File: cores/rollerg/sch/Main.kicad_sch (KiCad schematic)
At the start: 1 part, among them U1 053248

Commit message: wip rollerg sch: objects page
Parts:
- added D19, D20: 74LS257, symbol 74xx:74LS257
- added F11, F12: PAL16L8, symbol Logic_Programmable:PAL16L8
- added F13: 74LS138, symbol 74xx:74LS138
- added G18: 74LS174, symbol 74xx:74LS174
- added I16: ~, symbol konami:053252
- added J14: 74LS245, symbol jt74:74LS245
- renumbered U1 to H11
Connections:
- net VSS: now reaches H11.1 (VSS)
- net VSS: now also H11.10 (VSS), H11.19 (VSS), H11.25 (VSS), H11.31 (R0), H11.32 (R1), H11.33 (R2), H11.34 (R3), H11.35 (R4), H11.36 (R5), H11.37 (R6), H11.42 (VSS), H11.47 (R7), H11.48 (TEST), H11.5 (R9), H11.52 (R8), H11.57 (VSS), I16.22 (SEL0), I16.23 (SEL1), I16.28 (VSS), I16.43 (SEL2), I16.6 (VSS)
- net MAIN_A3: now reaches H11.11 (A3)
- net MAIN_A2: now reaches H11.12 (A2)
- net MAIN_A1: now reaches H11.13 (A1)
- net MAIN_A0: now reaches H11.14 (A0)
- net R/~{W}: now reaches H11.15 (R/~{W})
- net ~{AS}: now reaches H11.16 (~{AS})
- net ~{DS}: now reaches H11.20 (~{DS})
- net MAIN_D0: now reaches H11.21 (D0)
- net MAIN_D1: now reaches H11.22 (D1)
- net MAIN_D2: now reaches H11.23 (D2)
- net MAIN_D3: now reaches H11.24 (D3)
- net MAIN_D4: now reaches H11.27 (D4)
- net MAIN_D5: now reaches H11.28 (D5)
- net MAIN_D6: now reaches H11.29 (D6)
- net MAIN_D7: now reaches H11.30 (D7)
- net MAIN_A16: now reaches H11.38 (A16)
- net MAIN_A17: now reaches H11.39 (A17)
- net MAIN_A18: now reaches H11.40 (A18)
- net MAIN_A19: now reaches H11.41 (A19)
- net MAIN_A20: now reaches H11.43 (A20)
- net MAIN_A21: now reaches H11.44 (A21)
- net MAIN_A22: now reaches H11.45 (A22)
- net MAIN_A23: now reaches H11.46 (A23)
- net MAIN_A15: now reaches H11.53 (A15)
- net MAIN_A14: now reaches H11.54 (A14)
- net MAIN_A13: now reaches H11.55 (A13)
- net MAIN_A12: now reaches H11.56 (A12)
- net MAIN_A11: now reaches H11.59 (A11)
- net MAIN_A7: now reaches H11.6 (A7)
- net MAIN_A10: now reaches H11.60 (A10)
- net MAIN_A9: now reaches H11.61 (A9)
- net MAIN_A8: now reaches H11.62 (A8)
- net MAIN_A6: now reaches H11.7 (A6)
- net MAIN_A5: now reaches H11.8 (A5)
- net MAIN_A4: now reaches H11.9 (A4)
- new net: D19.12 (Zc), G18.13 (D4), J14.6 (A4)
- new net: D19.4 (Za), J14.9 (A7)
- new net: D19.7 (Zb), J14.8 (A6)
- new net: D19.9 (Zd), G18.14 (D5), J14.7 (A5)
- new net: D20.12 (Zc), G18.3 (D0), J14.2 (A0)
- new net: D20.4 (Za), G18.11 (D3), J14.5 (A3)
- new net: D20.7 (Zb), G18.6 (D2), J14.4 (A2)
- new net: D20.9 (Zd), G18.4 (D1), J14.3 (A1)
- new net: F13.14 (O1), G18.9 (Cp)
- new net: F12.2 (I2), G18.7 (Q2)
- new net DB0: I16.13 (DB0)
- new net DB1: I16.14 (DB1)
- new net DB2: I16.15 (DB2)
- new net DB3: I16.16 (DB3)
- new net DB4: I16.18 (DB4)
- new net DB5: I16.19 (DB5)
- new net DB6: I16.20 (DB6)
- new net DB7: I16.21 (DB7)
- new net G18P15: G18.15 (Q5)
- new net VCC: D20.11 (I0d), D20.14 (I0c), D20.2 (I0a), D20.5 (I0b)
- new net ~{OBJ_CS}: F12.18 (IO2)

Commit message: wip rollerg sch: PSAC progress
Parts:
- added J16: 74LS04, symbol jt74:74LS04
- added J17: XTAL_OSC, symbol Device:Crystal_GND23_Small
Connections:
- net VCC: now also J17.3
- net VSS: now also J17.1, J17.2
- net CLK4: now reaches I16.11 (CLK4)
- net ~{VBK}: now reaches I16.27 (~{VBK})
- net ~{HBK}: now reaches I16.33 (~{HBK})
- net at I16.5 (CLK): now also J16.4
- net RES: now reaches I16.7 (RES)
- net CLK1: now reaches I16.8 (CLK1)
- net CLK2: now reaches I16.9 (CLK2)
- net PAL14: now reaches F12.14 (IO6)
- net OBJOE: now reaches F12.16 (IO4)
- net PAL17: now reaches F12.17 (I03)
- net OBJSE: now reaches F12.19 (IO1)
- new net 24CLK: J16.3, J17.4

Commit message: wip rollerg sch: PSAC
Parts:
- added C20, C21, C23: 74LS253, symbol 74xx:74LS253
- added D18, G16: 74LS32, symbol jt74:74LS32
- added DIPSW2: SW_DIP_x08, symbol Switch:SW_DIP_x08
- added F11: PAL16L8, symbol Logic_Programmable:PAL16L8
- added F14: 74LS04, symbol jt74:74LS04
- added F16: 74LS08, symbol 74xx:74LS08
- added RA4_7KX8: R_Network08_US, Resistor_THT:R_Array_SIP7, symbol Device:R_Network08_US
- added S1: 051550, symbol konami:051550
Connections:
- net MAIN_A0: now also D18.5, F14.3
- net MAIN_A10: now also F12.5 (I5)
- net MAIN_A11: now also F12.4 (I4)
- net MAIN_A12: now also F12.3 (I3)
- net MAIN_A4: now also F13.1 (A0)
- net MAIN_A5: now also F12.11 (I10), F13.2 (A1)
- net MAIN_A6: now also F12.9 (I9), F13.3 (A2)
- net MAIN_A7: now also F12.8 (I8)
- net MAIN_A8: now also F12.7 (I7)
- net MAIN_A9: now also F12.6 (I6)
- net OBJSE: now also D18.4
- net VCC: now also D19.11 (I0d), D19.14 (I0c), D19.5 (I0b), F13.6 (E3)
- net VSS: now also F13.5 (E2), C20.10 (I0b), C20.6 (I0a), C21.10 (I0b), C21.11 (I1b), C21.6 (I0a), C23.10 (I0b), C23.11 (I1b), C23.6 (I0a), S1.13 (VSS), S1.14 (VSS)
- net ~{DS}: now also D18.10
- net ~{OBJ_CS}: now also F16.10
- net at D19.1 (S): now also D20.1 (S), F14.4
- net at D19.10 (I1d): now also DIPSW2.11, RA4_7KX8.7 (R6)
- net MAIN_Z6: now reaches D19.12 (Zc), G18.13 (D4), J14.6 (A4)
- net at D19.13 (I1c): now also DIPSW2.12, RA4_7KX8.6 (R5)
- net ZOE: now reaches D19.15 (OE)
- net ZOE: now also F13.9 (O6)
- net CPU~{EN}: now reaches D19.2 (I0a)
- net CPU~{EN}: now also G16.2
- net at D19.3 (I1a): now also DIPSW2.9, RA4_7KX8.9 (R8)
- net MAIN_Z4: now reaches D19.4 (Za), J14.9 (A7)
- net at D19.6 (I1b): now also DIPSW2.10, RA4_7KX8.8 (R7)
- net MAIN_Z5: now reaches D19.7 (Zb), J14.8 (A6)
- net MAIN_Z7: now reaches D19.9 (Zd), G18.14 (D5), J14.7 (A5)
- net at D20.10 (I1d): now also DIPSW2.15, RA4_7KX8.3 (R2)
- net MAIN_Z2: now reaches D20.12 (Zc), G18.3 (D0), J14.2 (A0)
- net at D20.13 (I1c): now also DIPSW2.16, RA4_7KX8.2 (R1)
- net at D20.15 (OE): now also F11.9 (I9)
- net at D20.3 (I1a): now also DIPSW2.13, RA4_7KX8.5 (R4)
- net MAIN_Z0: now reaches D20.4 (Za), G18.11 (D3), J14.5 (A3)
- net at D20.6 (I1b): now also DIPSW2.14, RA4_7KX8.4 (R3)
- net MAIN_Z1: now reaches D20.7 (Zb), G18.6 (D2), J14.4 (A2)
- net MAIN_Z3: now reaches D20.9 (Zd), G18.4 (D1), J14.3 (A1)
- net CRES: now reaches I16.12 (CRES)
- net CRES: now also G18.1 (~{Mr})
- net DTAC: now reaches H11.49 (DTAC)
- net at F13.10 (O5): now also C20.1 (OEa), C20.15 (OEb), C21.1 (OEa), C21.15 (OEb), C23.1 (OEa), C23.15 (OEb)
- net PAL12: now reaches F13.4 (E1)
- net PAL12: now also F12.12 (IO8)
- net at J14.1 (A->B): now also G16.11
- net OBJRAMD7: now reaches J14.11 (B7)
- net OBJRAMD6: now reaches J14.12 (B6)
- net OBJRAMD5: now reaches J14.13 (B5)
- net OBJRAMD4: now reaches J14.14 (B4)
- net OBJRAMD3: now reaches J14.15 (B3)
- net OBJRAMD2: now reaches J14.16 (B2)
- net OBJRAMD1: now reaches J14.17 (B1)
- net OBJRAMD0: now reaches J14.18 (B0)
- net at J14.19 (~{CE}): now also G16.3
- net at F12.1 (I1): now also F11.12 (IO8)
- net PAL15: now reaches F12.15 (IO5)
- net PAL15: now also F14.5, F16.9
- net G18P7: now reaches F12.2 (I2), G18.7 (Q2)
- net at G18.2 (Q0): now also S1.15 (OUT1)
- net at G18.5 (Q1): now also S1.16 (OUT2)
- new net: F16.8, G16.1
- new net: F14.6, G16.12
- new net: D18.6, D18.9
- new net WR: D18.8
- new net ~{RD}: G16.13
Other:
- moved on the sheet: F11, F12

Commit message: wip rollerg sch: SOUND
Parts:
- removed C20, C21, C23: 74LS253, symbol 74xx:74LS253
- removed F11: PAL16L8, symbol Logic_Programmable:PAL16L8
- removed unit 3 of F14
- removed F16: 74LS08, symbol 74xx:74LS08
- removed G16: 74LS32, symbol jt74:74LS32
- removed J14: 74LS245, symbol jt74:74LS245
- added 7KX4: R_Network04_US, Resistor_THT:R_Array_SIP5, symbol Device:R_Network04_US
- added C18, D16: 74LS07, symbol 74xx:74LS07
- added F9: 74LS245, symbol jt74:74LS245
- added H14: 74LS367, symbol 74xx:74LS367
- added H16: 74LS04, symbol jt74:74LS04
- added JP2: Jumper_2_Open, symbol Jumper:Jumper_2_Open
- added R1: 222, symbol Device:R_US
- added R10, R17: 470, symbol Device:R_US
- added R11, R5: 100, symbol Device:R_US
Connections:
- net CRES: now also H14.4 (I2)
- net DB0: now also G18.3 (D0), F9.2 (A0)
- net DB1: now also G18.4 (D1), F9.3 (A1)
- net DB2: now also G18.6 (D2), F9.4 (A2)
- net DB3: now also G18.11 (D3), F9.5 (A3)
- net DB4: now also G18.13 (D4), F9.6 (A4)
- net DB5: now also G18.14 (D5), F9.7 (A5)
- net DB6: now also F9.8 (A6)
- net DB7: now also F9.9 (A7)
- net MAIN_A0: now also I16.42 (AB0)
- net MAIN_A1: now also I16.41 (AB1)
- net MAIN_A12: now also F11.5 (I5)
- net MAIN_A13: now also F11.4 (I4)
- net MAIN_A14: now also F11.3 (I3)
- net MAIN_A15: now also F11.2 (I2)
- net MAIN_A16: now also F11.9 (I9)
- net MAIN_A17: now also F11.8 (I8)
- net MAIN_A18: now also F11.7 (I7)
- net MAIN_A19: now also F11.6 (I6)
- net MAIN_A2: now also I16.40 (AB2)
- net MAIN_A3: now also I16.38 (AB3)
- net MAIN_D0: now also F9.18 (B0)
- net MAIN_D1: now also F9.17 (B1)
- net MAIN_D2: now also F9.16 (B2)
- net MAIN_D3: now also F9.15 (B3)
- net MAIN_D4: now also F9.14 (B4)
- net MAIN_D5: now also F9.13 (B5)
- net MAIN_D6: now also F9.12 (B6)
- net MAIN_D7: now also F9.11 (B7)
- net MAIN_Z0: no longer G18.11 (D3)
- net MAIN_Z1: no longer G18.6 (D2)
- net MAIN_Z2: no longer G18.3 (D0)
- net MAIN_Z3: no longer G18.4 (D1)
- net MAIN_Z6: no longer G18.13 (D4)
- net MAIN_Z7: no longer G18.14 (D5)
- net RES: now also S1.10 (~{RESET})
- net R/~{W}: now also F11.11 (I10), I16.37 (~{RW}), F9.1 (A->B)
- net VCC: now also D19.16 (VCC), D20.16 (VCC), F11.20 (VCC), F13.16 (VCC), H11.26 (VCC), H11.50 (EPA), H11.58 (VCC), I16.17 (VDD), I16.3 (~{HLDI}), I16.39 (VDD), I16.4 (~{VLDI}), 7KX4.1 (common), H14.16 (VCC), R10.2, R17.2
- net VSS: now also D19.8 (GND), D20.8 (GND), F11.10 (GND), F13.8 (GND), 7KX4.2 (R1), 7KX4.3 (R2), 7KX4.4 (R3), 7KX4.5 (R4), H14.1 (OEa), H14.8 (GND), R1.1
- net ZOE: now also D20.15 (OE)
- net ~{AS}: now also F11.1 (I1)
- net MOE: now reaches F13.10 (O5)
- net SMU: now reaches D19.1 (S), D20.1 (S), F14.4
- net ~{CS1}: now reaches F11.13 (IO7)
- net MAIN_AB0: now reaches F11.14 (IO6)
- net MAIN_AB1: now reaches F11.15 (IO5)
- net MAIN_AB2: now reaches F11.16 (IO4)
- net MAIN_AB3: now reaches F11.17 (I03)
- net at F11.18 (IO2): now also F9.19 (~{CE})
- net OOE: now reaches F11.19 (IO1)
- net PE: now reaches I16.1 (PE)
- net PE: now also H14.2 (I1)
- net PQ: now reaches I16.2 (PQ)
- net PQ: now also H16.5
- net at I16.25 (~{CSY}): now also D16.1
- net at I16.26 (~{VSY}): now also C18.5
- net ~{IRQ}: now reaches I16.34 (INT1)
- net ~{IRQ}: now also H11.4 (~{IRQ})
- net ~{CCO}: now reaches I16.36 (~{CC0})
- net ~{CCO}: now also F12.13 (IO7)
- net MPQ: now reaches H11.17 (PQ)
- net MPQ: now also H14.3 (O1a)
- net ~{CLK2}: now reaches H11.18 (CLK)
- net RESET: now reaches H11.2 (~{RESET})
- net RESET: now also H14.5 (O2a)
- net MPE: now reaches H11.51 (PE)
- net MPE: now also H14.7 (O3a)
- net RCLK: now reaches S1.1 (CLK)
- net RCLK: now also F13.13 (O2)
- net COIN_CNT_2: now reaches S1.20 (CNT2)
- net COIN_CNT_2: now also S1.21 (CNT2)
- net COIN_CNT_1: now reaches S1.22 (CNT1)
- net COIN_CNT_1: now also S1.23 (CNT1)
- net at S1.4 (VREF): now also JP2.2 (B)
- net at S1.5 (RES): now also JP2.1 (A)
- net at S1.7 (CT): now also R1.2
- net SND_INT: now reaches F13.11 (O4)
- net ~{MCS}: now reaches F13.12 (O3)
- new net: D16.2, R10.1, R5.1
- new net: H14.6 (I3), H16.6
- new net: C18.6, R11.1, R17.1
- new net SYNC: R5.2
- no-connect marks 0 -> 8
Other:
- note added: "PULL"
- moved on the sheet: D18B, D18C, D19, D20, DIPSW2, F11, F12, F13, F14B, G18, H11, I16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

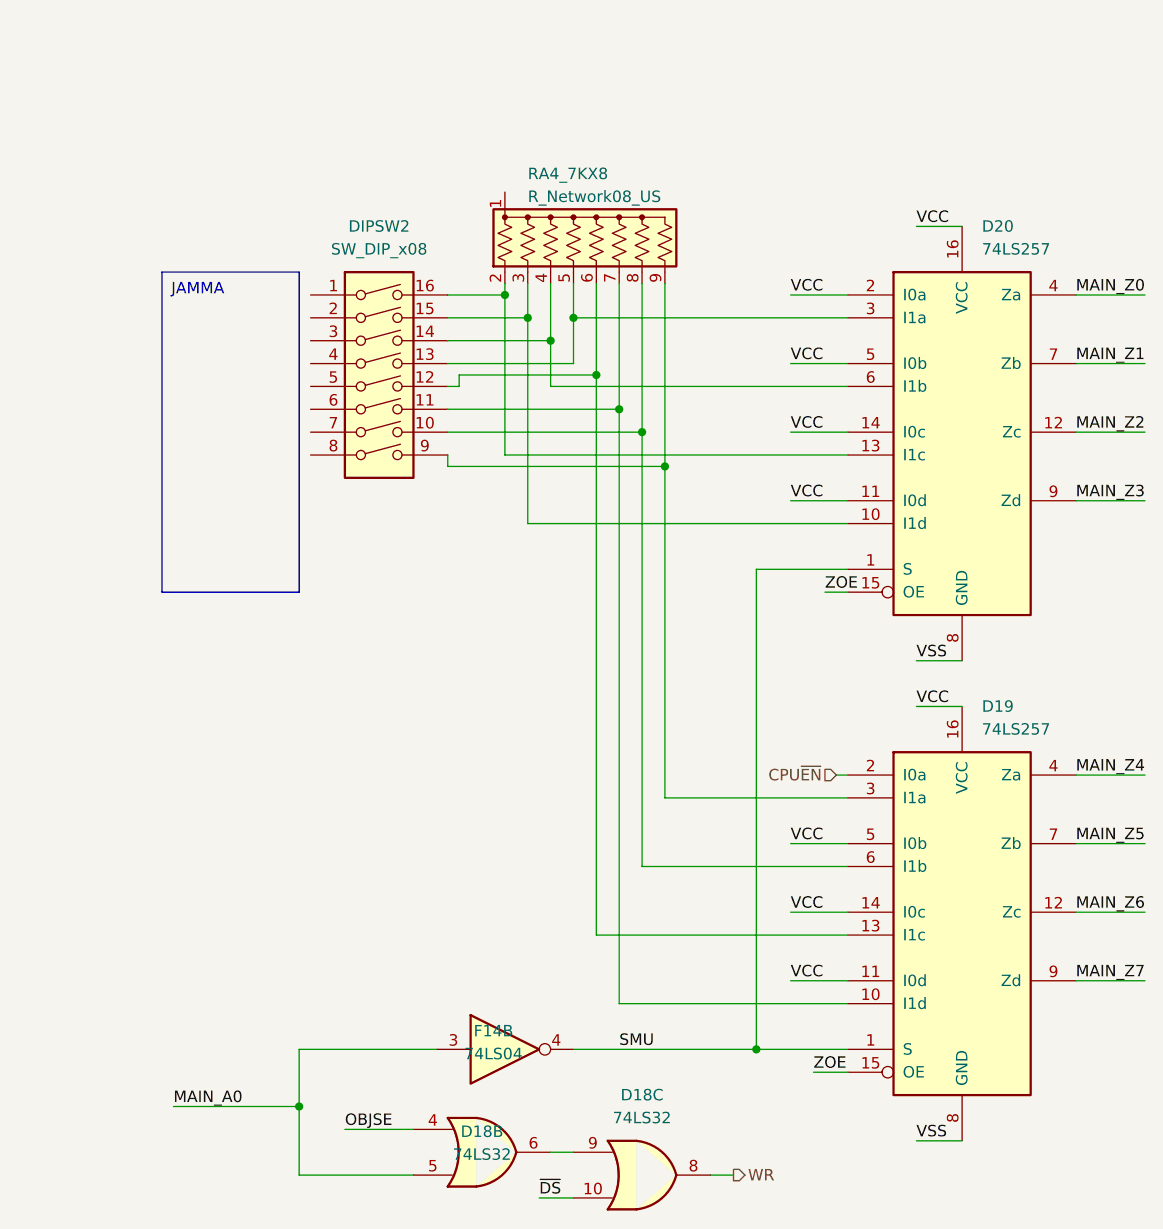
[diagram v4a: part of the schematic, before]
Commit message: wip rollerg sch: CABINET AND RGB
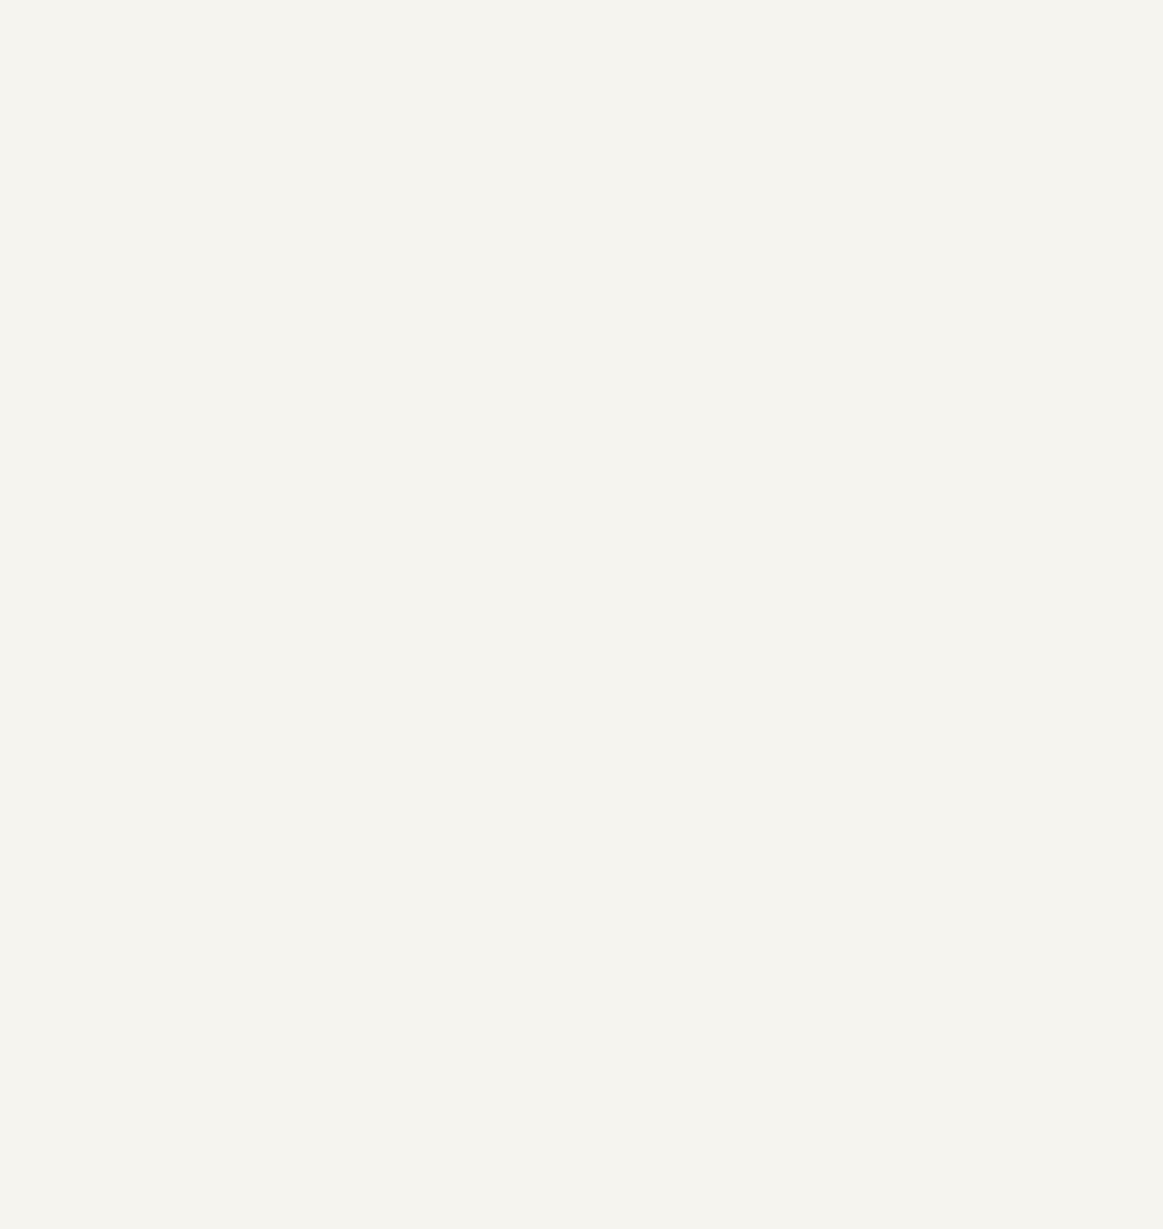
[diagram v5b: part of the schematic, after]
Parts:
- removed D18: 74LS32, symbol jt74:74LS32
- removed D19, D20: 74LS257, symbol 74xx:74LS257
- removed DIPSW2: SW_DIP_x08, symbol Switch:SW_DIP_x08
- removed F14: 74LS04, symbol jt74:74LS04
- removed RA4_7KX8: R_Network08_US, Resistor_THT:R_Array_SIP7, symbol Device:R_Network08_US

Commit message: almost complete rollerg sch
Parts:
- removed 7KX4: R_Network04_US, Resistor_THT:R_Array_SIP5, symbol Device:R_Network04_US
- removed R1: 222, symbol Device:R_US
- added C6: 100k, Capacitor_THT:C_Axial_L3.8mm_D2.6mm_P10.00mm_Horizontal, symbol Device:C
- added RN7: R_Network08_US, Resistor_THT:R_Array_SIP9, symbol Device:R_Network08_US
- renumbered R5 to R9
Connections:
- net MPE: now also RN7.8 (R7)
- net MPQ: now also RN7.9 (R8)
- net RESET: now also RN7.2 (R1)
- net VCC: now also F12.20 (VCC), G18.16 (VCC), RN7.1 (common)
- net VSS: now also F12.10 (GND), G18.8 (GND), C6.2
- net ~{IRQ}: now also RN7.6 (R5)
- net at S1.7 (CT): now also C6.1
- net ~{VSYNC}: now reaches C18.5, I16.26 (~{VSY})
- net ~{HSYNC}: now reaches I16.29 (~{HSY})
- net at H11.3 (~{NMI}): now also RN7.7 (R6)
- net at H11.63 (~{FIRQ}): now also RN7.5 (R4)
- net at H11.64 (~{HALT}): now also RN7.3 (R2)
- net +12V: now reaches S1.19 (+12V)
- net +5V: now reaches S1.9 (+5V)
- net MAIN_A20: no longer names the net of H11.43 (A20)
- net MAIN_A21: no longer names the net of H11.44 (A21)
- net MAIN_A22: no longer names the net of H11.45 (A22)
- net MAIN_A23: no longer names the net of H11.46 (A23)
- net PAL15 renamed ~{OBJSET}
- no-connect marks 8 -> 24
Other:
- note removed: "PULL"
- moved on the sheet: F11, F12, F13, F9, G18, H11, H14, H16C, JP2, R11, R17, S1

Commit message: unpopulated sheet
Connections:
- net ~{HALT}: now reaches H11.64 (~{HALT}), RN7.3 (R2)
- net ~{FIRQ}: now reaches H11.63 (~{FIRQ}), RN7.5 (R4)
- net ~{NMI}: now reaches H11.3 (~{NMI}), RN7.7 (R6)
- net MAIN_A20: now reaches H11.43 (A20)
- net MAIN_A21: now reaches H11.44 (A21)
- net MAIN_A22: now reaches H11.45 (A22)
- net MAIN_A23: now reaches H11.46 (A23)
- no-connect marks 24 -> 20
